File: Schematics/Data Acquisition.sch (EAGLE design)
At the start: 22 parts, among them J1 TERMBLOCK_1X2-3.5MM, U1 INA219BIDCNT, U2 INA169

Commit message: added some pluggery
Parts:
- removed CATHODE_ONE: (no value), con-phoenix-254:MPT2
- removed Q1: (no value), adafruit:MOSFET-NGDS_TO220V
- added R9: 4k7, rcl:R-US_0207/10
- added X2: D-SUB9-H2M09ST, con-thomas-betts:D-SUB9-H2M09ST
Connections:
- removed net N$3: CATHODE_ONE-2.1, Q1.D
- removed net V+: J1.2, R5.2, U1.VIN+
- new net 1-WIRE: PCB1.9, R9.1, X2-6.F
- net GND: now also X2-4.F, X2-5.F; no longer Q1.S
- net KATH-1: no longer Q1.G
- net SCL: now also X2-3.F
- net SDA: now also X2-2.F
- net VCC: now also R9.2, X2-1.F, X2-7.F
- net VIN+: now also J1.2, R5.2, U1.VIN+
- net VIN-: no longer CATHODE_ONE-1.1
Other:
- note added: "BLACK"
- note added: "GREEN"
- note added: "GREY"
- note added: "ORANGE"
- note added: "PURPLE"
- note added: "WHITE"
- note added: "YELLOW"

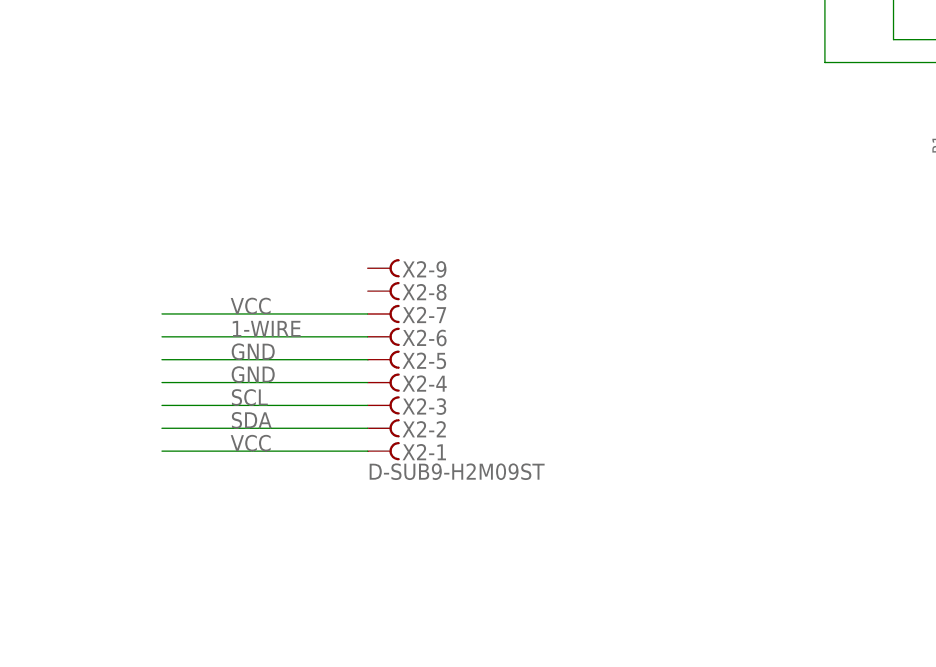
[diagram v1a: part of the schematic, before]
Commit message: Temp sense and H bridge
plug for temp sensor wiring for H bridge to arduino
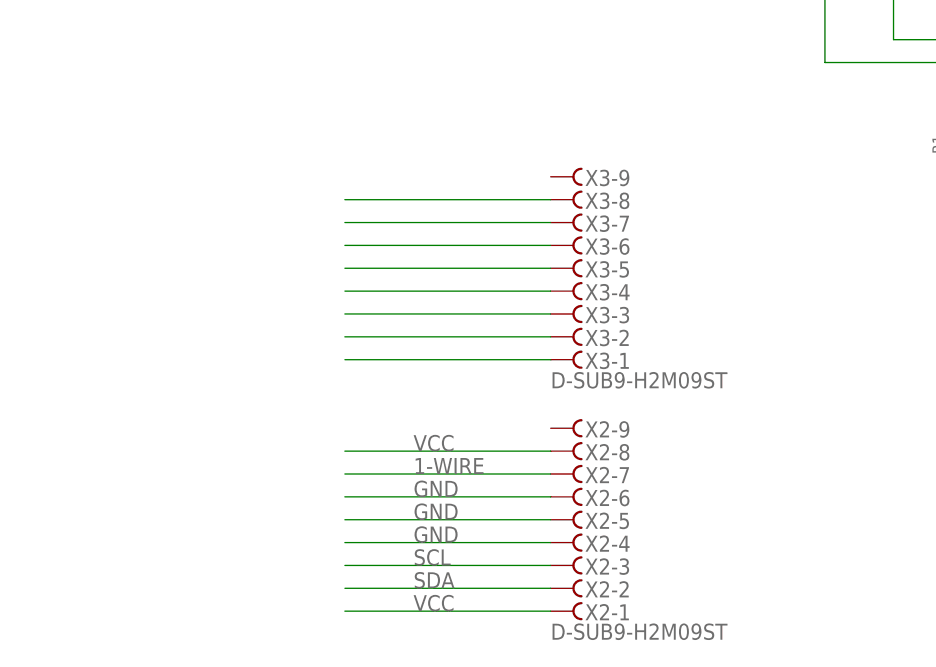
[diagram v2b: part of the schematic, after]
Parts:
- added X3: D-SUB9-H2M09ST, con-thomas-betts:D-SUB9-H2M09ST
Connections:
- new net N$10: X3-8.F
- new net N$3: X3-1.F
- new net N$4: X3-2.F
- new net N$5: X3-3.F
- new net N$6: X3-4.F
- new net N$7: X3-5.F
- new net N$8: X3-6.F
- new net N$9: X3-7.F
- net 1-WIRE: now also X2-7.F; no longer X2-6.F
- net GND: now also X2-6.F
- net VCC: now also X2-8.F; no longer X2-7.F
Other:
- note added: "BLUE"
- note added: "CABLE SIDE"
- note added: "PLUG SIDE"
- note added: "RED"
- note added: "Shield"
- moved on the sheet: X2-1, X2-2, X2-3, X2-4, X2-5, X2-6, X2-7, X2-8, X2-9
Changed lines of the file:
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@@
 <part name="R9" library="rcl" library_urn="urn:adsk.eagle:library:334" deviceset="R-US_" device="0207/10" package3d_urn="urn:adsk.eagle:package:23491/1" value="4k7"/>
 <part name="P+11" library="microbuilder" deviceset="VCC" device=""/>
+<part name="X3" library="con-thomas-betts" library_urn="urn:adsk.eagle:library:191" deviceset="D-SUB9-" device="H2M09ST" package3d_urn="urn:adsk.eagle:package:10567/1"/>
 </parts>
 <sheets>
@@
 <text x="251.46" y="195.58" size="1.778" layer="94">Vout = Iload * Rload * Rshunt / 1000</text>
 <text x="251.46" y="190.5" size="1.778" layer="94">Vout = 1Volt per1 Amp</text>
-<text x="157.48" y="35.56" size="1.4224" layer="90">GREEN</text>
-<text x="154.94" y="38.1" size="1.4224" layer="90">YELLOW</text>
-<text x="154.94" y="40.64" size="1.4224" layer="90">ORANGE</text>
-<text x="157.48" y="33.02" size="1.4224" layer="90">BLACK</text>
-<text x="157.48" y="30.48" size="1.4224" layer="90">WHITE</text>
-<text x="157.48" y="27.94" size="1.4224" layer="90">GREY</text>
-<text x="154.94" y="25.4" size="1.4224" layer="90">PURPLE</text>
+<text x="177.8" y="20.32" size="1.4224" layer="90">GREEN</text>
+<text x="175.26" y="22.86" size="1.4224" layer="90">YELLOW</text>
+<text x="175.26" y="25.4" size="1.4224" layer="90">ORANGE</text>
+<text x="177.8" y="15.24" size="1.4224" layer="90">BLACK</text>
+<text x="177.8" y="12.7" size="1.4224" layer="90">WHITE</text>
+<text x="177.8" y="10.16" size="1.4224" layer="90">GREY</text>
+<text x="175.26" y="7.62" size="1.4224" layer="90">PURPLE</text>
+<text x="175.26" y="17.78" size="1.778" layer="90">Shield</text>
+<text x="177.8" y="35.56" size="1.778" layer="90">RED</text>
+<text x="177.8" y="43.18" size="1.778" layer="90">BLUE</text>
+<text x="177.8" y="38.1" size="1.778" layer="90">GREEN</text>
+<text x="177.8" y="40.64" size="1.778" layer="90">YELLOW</text>
+<text x="177.8" y="53.34" size="1.778" layer="90">RED</text>
+<text x="177.8" y="48.26" size="1.778" layer="90">BLUE</text>
+<text x="210.82" y="45.72" size="1.778" layer="90">CABLE SIDE</text>
+<text x="210.82" y="17.78" size="1.778" layer="90">PLUG SIDE</text>
+<text x="177.8" y="50.8" size="1.778" layer="90">YELLOW</text>
 </plain>
 <instances>
@@
 <instance part="X1" gate="-1" x="302.26" y="165.1"/>
 <instance part="X1" gate="-2" x="302.26" y="160.02"/>
-<instance part="X2" gate="-1" x="182.88" y="25.4" rot="MR180"/>
-<instance part="X2" gate="-2" x="182.88" y="27.94" rot="MR180"/>
-<instance part="X2" gate="-3" x="182.88" y="30.48" rot="MR180"/>
-<instance part="X2" gate="-4" x="182.88" y="33.02" rot="MR180"/>
-<instance part="X2" gate="-5" x="182.88" y="35.56" rot="MR180"/>
-<instance part="X2" gate="-6" x="182.88" y="38.1" rot="MR180"/>
-<instance part="X2" gate="-7" x="182.88" y="40.64" rot="MR180"/>
-<instance part="X2" gate="-8" x="182.88" y="43.18" rot="MR180"/>
-<instance part="X2" gate="-9" x="182.88" y="45.72" rot="MR180"/>
+<instance part="X2" gate="-1" x="203.2" y="7.62" rot="MR180"/>
+<instance part="X2" gate="-2" x="203.2" y="10.16" rot="MR180"/>
+<instance part="X2" gate="-3" x="203.2" y="12.7" rot="MR180"/>
+<instance part="X2" gate="-4" x="203.2" y="15.24" rot="MR180"/>
+<instance part="X2" gate="-5" x="203.2" y="17.78" rot="MR180"/>
+<instance part="X2" gate="-6" x="203.2" y="20.32" rot="MR180"/>
+<instance part="X2" gate="-7" x="203.2" y="22.86" rot="MR180"/>
+<instance part="X2" gate="-8" x="203.2" y="25.4" rot="MR180"/>
+<instance part="X2" gate="-9" x="203.2" y="27.94" rot="MR180"/>
 <instance part="R9" gate="G$1" x="175.26" y="170.18" rot="R90"/>
 <instance part="P+11" gate="VCC" x="175.26" y="177.8"/>
+<instance part="X3" gate="-1" x="203.2" y="35.56" rot="MR180"/>
+<instance part="X3" gate="-2" x="203.2" y="38.1" rot="MR180"/>
+<instance part="X3" gate="-3" x="203.2" y="40.64" rot="MR180"/>
+<instance part="X3" gate="-4" x="203.2" y="43.18" rot="MR180"/>
+<instance part="X3" gate="-5" x="203.2" y="45.72" rot="MR180"/>
+<instance part="X3" gate="-6" x="203.2" y="48.26" rot="MR180"/>
+<instance part="X3" gate="-7" x="203.2" y="50.8" rot="MR180"/>
+<instance part="X3" gate="-8" x="203.2" y="53.34" rot="MR180"/>
+<instance part="X3" gate="-9" x="203.2" y="55.88" rot="MR180"/>
 </instances>
 <busses>
@@
 <segment>
 <pinref part="X2" gate="-1" pin="F"/>
-<wire x1="180.34" y1="25.4" x2="157.48" y2="25.4" width="0.1524" layer="91"/>
-<label x="165.1" y="25.4" size="1.778" layer="95"/>
-</segment>
-<segment>
-<pinref part="X2" gate="-7" pin="F"/>
-<wire x1="180.34" y1="40.64" x2="157.48" y2="40.64" width="0.1524" layer="91"/>
-<label x="165.1" y="40.64" size="1.778" layer="95"/>
+<wire x1="200.66" y1="7.62" x2="177.8" y2="7.62" width="0.1524" layer="91"/>
+<label x="185.42" y="7.62" size="1.778" layer="95"/>
 </segment>
 <segment>
 <pinref part="R9" gate="G$1" pin="2"/>
 <pinref part="P+11" gate="VCC" pin="VCC"/>
+</segment>
+<segment>
+<pinref part="X2" gate="-8" pin="F"/>
+<wire x1="200.66" y1="25.4" x2="177.8" y2="25.4" width="0.1524" layer="91"/>
+<label x="185.42" y="25.4" size="1.778" layer="95"/>
 </segment>
 </net>
@@
 <segment>
 <pinref part="X2" gate="-4" pin="F"/>
-<wire x1="180.34" y1="33.02" x2="157.48" y2="33.02" width="0.1524" layer="91"/>
-<label x="165.1" y="33.02" size="1.778" layer="95"/>
+<wire x1="200.66" y1="15.24" x2="177.8" y2="15.24" width="0.1524" layer="91"/>
+<label x="185.42" y="15.24" size="1.778" layer="95"/>
 </segment>
 <segment>
 <pinref part="X2" gate="-5" pin="F"/>
-<wire x1="180.34" y1="35.56" x2="157.48" y2="35.56" width="0.1524" layer="91"/>
-<label x="165.1" y="35.56" size="1.778" layer="95"/>
+<wire x1="200.66" y1="17.78" x2="177.8" y2="17.78" width="0.1524" layer="91"/>
+<label x="185.42" y="17.78" size="1.778" layer="95"/>
+</segment>
+<segment>
+<pinref part="X2" gate="-6" pin="F"/>
+<wire x1="200.66" y1="20.32" x2="177.8" y2="20.32" width="0.1524" layer="91"/>
+<label x="185.42" y="20.32" size="1.778" layer="95"/>
 </segment>
 </net>
@@
 <segment>
 <pinref part="X2" gate="-2" pin="F"/>
-<wire x1="180.34" y1="27.94" x2="157.48" y2="27.94" width="0.1524" layer="91"/>
-<label x="165.1" y="27.94" size="1.778" layer="95"/>
+<wire x1="200.66" y1="10.16" x2="177.8" y2="10.16" width="0.1524" layer="91"/>
+<label x="185.42" y="10.16" size="1.778" layer="95"/>
 </segment>
 </net>
@@
 <segment>
 <pinref part="X2" gate="-3" pin="F"/>
-<wire x1="180.34" y1="30.48" x2="157.48" y2="30.48" width="0.1524" layer="91"/>
-<label x="165.1" y="30.48" size="1.778" layer="95"/>
+<wire x1="200.66" y1="12.7" x2="177.8" y2="12.7" width="0.1524" layer="91"/>
+<label x="185.42" y="12.7" size="1.778" layer="95"/>
 </segment>
 </net>
@@
 <net name="1-WIRE" class="0">
 <segment>
-<pinref part="X2" gate="-6" pin="F"/>
-<wire x1="180.34" y1="38.1" x2="157.48" y2="38.1" width="0.1524" layer="91"/>
-<label x="165.1" y="38.1" size="1.778" layer="95"/>
-</segment>
-<segment>
 <pinref part="PCB1" gate="G$1" pin="9"/>
 <wire x1="147.32" y1="165.1" x2="175.26" y2="165.1" width="0.1524" layer="91"/>
@@
 <pinref part="R9" gate="G$1" pin="1"/>
 </segment>
-</net>
+<segment>
+<pinref part="X2" gate="-7" pin="F"/>
+<wire x1="200.66" y1="22.86" x2="177.8" y2="22.86" width="0.1524" layer="91"/>
+<label x="185.42" y="22.86" size="1.778" layer="95"/>
+</segment>
+</net>
+<net name="N$3" class="0">
+<segment>
+<pinref part="X3" gate="-1" pin="F"/>
+<wire x1="200.66" y1="35.56" x2="177.8" y2="35.56" width="0.1524" layer="91"/>
+</segment>
+</net>
+<net name="N$4" class="0">
+<segment>
+<pinref part="X3" gate="-2" pin="F"/>
+<wire x1="200.66" y1="38.1" x2="177.8" y2="38.1" width="0.1524" layer="91"/>
+</segment>
+</net>
+<net name="N$5" class="0">
+<segment>
+<pinref part="X3" gate="-3" pin="F"/>
+<wire x1="200.66" y1="40.64" x2="177.8" y2="40.64" width="0.1524" layer="91"/>
+</segment>
+</net>
+<net name="N$6" class="0">
+<segment>
+<pinref part="X3" gate="-4" pin="F"/>
+<wire x1="200.66" y1="43.18" x2="177.8" y2="43.18" width="0.1524" layer="91"/>
+</segment>
+</net>
+<net name="N$7" class="0">
+<segment>
+<pinref part="X3" gate="-5" pin="F"/>
+<wire x1="200.66" y1="45.72" x2="177.8" y2="45.72" width="0.1524" layer="91"/>
+</segment>
+</net>
+<net name="N$8" class="0">
+<segment>
+<pinref part="X3" gate="-6" pin="F"/>
+<wire x1="200.66" y1="48.26" x2="177.8" y2="48.26" width="0.1524" layer="91"/>
+</segment>
+</net>
+<net name="N$9" class="0">
+<segment>
+<pinref part="X3" gate="-7" pin="F"/>
+<wire x1="200.66" y1="50.8" x2="177.8" y2="50.8" width="0.1524" layer="91"/>
+</segment>
+</net>
+<net name="N$10" class="0">
+<segment>
+<pinref part="X3" gate="-8" pin="F"/>
+<wire x1="200.66" y1="53.34" x2="177.8" y2="53.34" width="0.1524" layer="91"/>
+</segment>
+</net>
